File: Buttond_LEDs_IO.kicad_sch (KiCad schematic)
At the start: 16 parts, among them J12 SFH11-PBPC-D05-ST-BK, J13 SFH11-PBPC-D05-ST-BK, SW1 RESET, SW2 BOOT

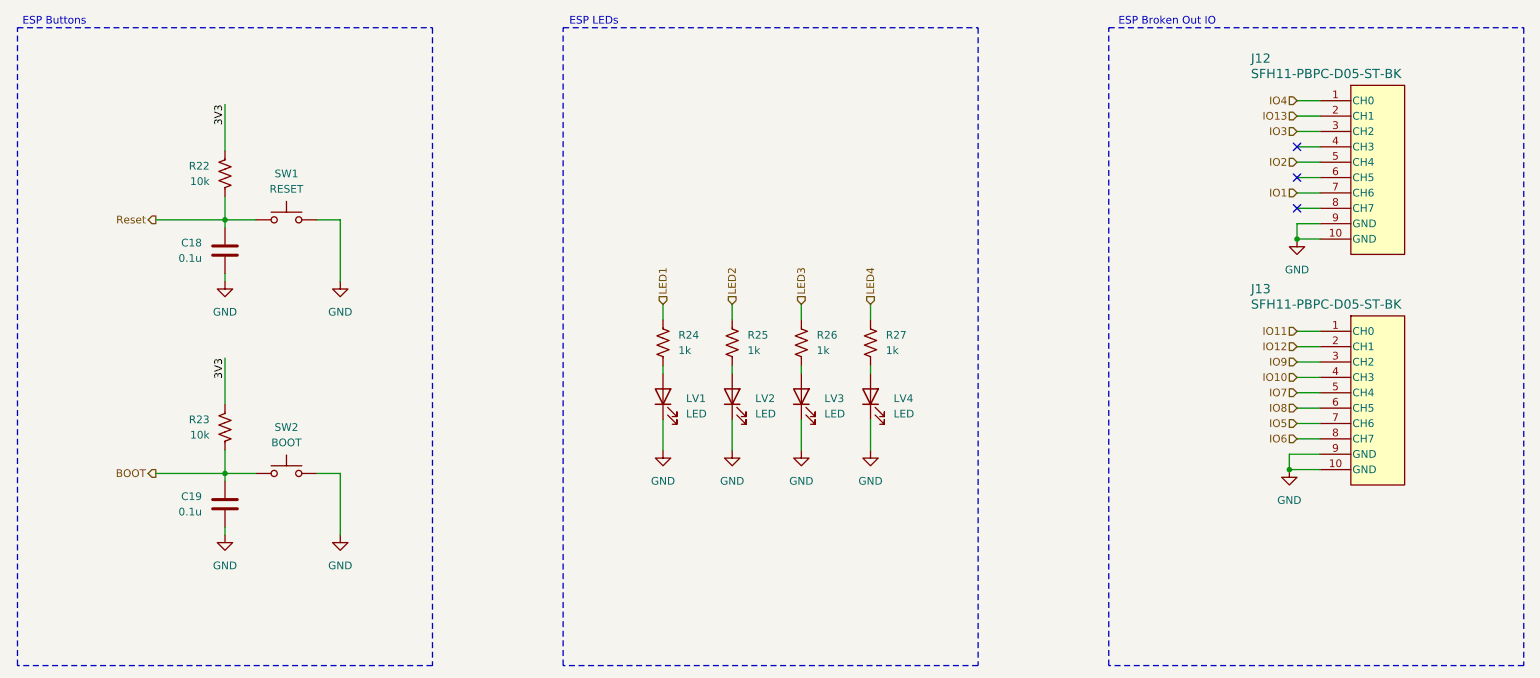
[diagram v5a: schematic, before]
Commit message: changed rpp ic
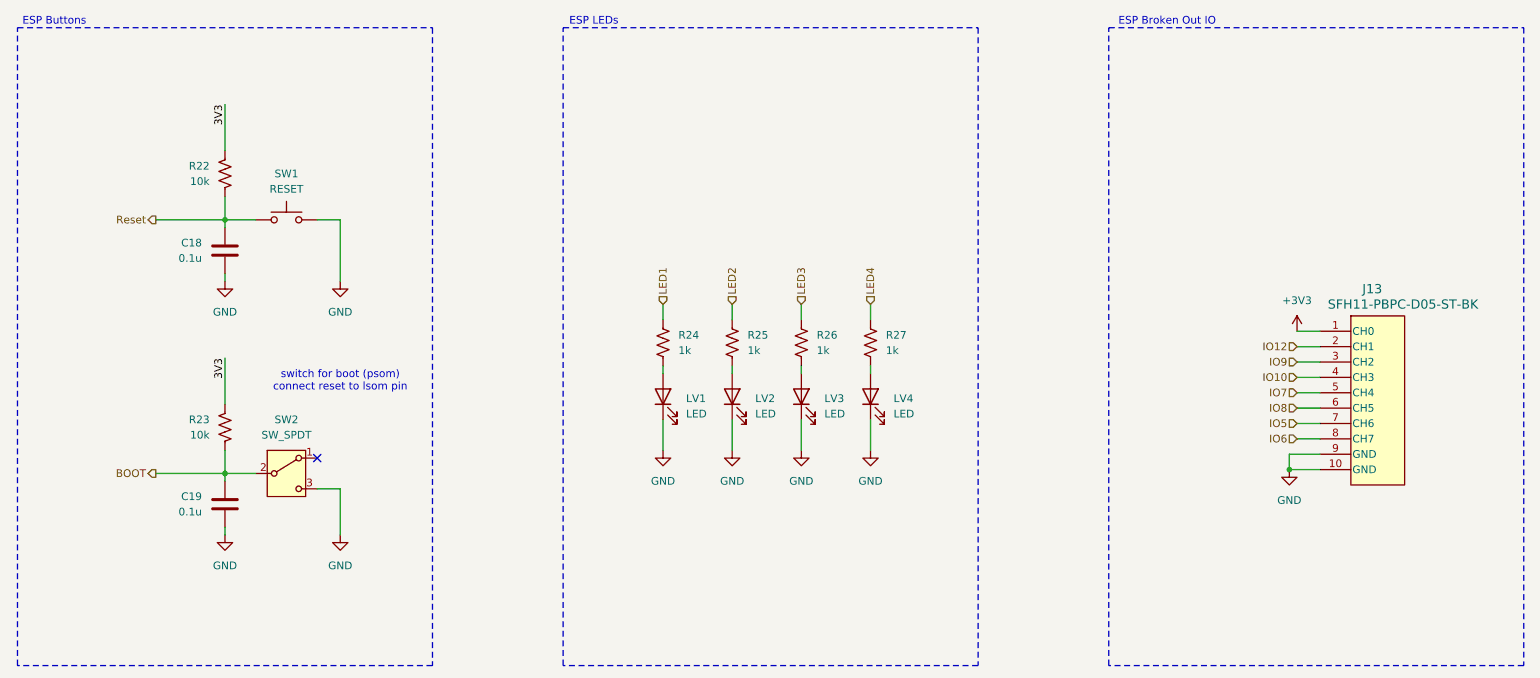
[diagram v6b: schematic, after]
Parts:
- removed J12: SFH11-PBPC-D05-ST-BK, UTSVT_Connectors:CONN_SFH11-xxxC-D05-ST-XX_SUL, symbol UTSVT_Connectors:SFH11-PBPC-D05-ST-BK
- removed SW2: BOOT, UTSVT_Special:SW_SPST_B3SL-1002P, symbol Switch:SW_MEC_5G
- added SW2: SW_SPDT, symbol Switch:SW_SPDT
- J13: P/N (none) -> SFH11-PBPC-D05-ST-BK
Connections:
- net BOOT: now also SW2.2 (B)
- net GND: now also SW2.3 (C)
- net IO11 renamed +3V3
- no-connect marks 3 -> 1
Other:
- note added: "switch for boot (psom) connect reset to lsom pin"

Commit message: as;ldfkjasdl;f
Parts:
- removed C19: 0.1u, Capacitor_SMD:C_0603_1608Metric, symbol Device:C
- SW2: value SW_SPDT -> BOOT; footprint (none) -> UTSVT_Special:SW_CJS-1200TA
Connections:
- net +3V3: now also R22.1, SW2.1 (A)
- net BOOT: now also R23.1; no longer R23.2, SW2.2 (B)
- removed net 3V3: R22.1, R23.1
- new net: R23.2, SW2.2 (B)
- no-connect marks 1 -> 0
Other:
- moved on the sheet: R23
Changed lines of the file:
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@@
-	)
-	(junction
-		(at 60.96 105.41)
-		(diameter 0)
-		(color 0 0 0 0)
 	)
 	(junction
@@
 		(color 0 0 0 0)
 	)
-	(no_connect
-		(at 76.2 102.87)
-	)
 	(wire
 		(pts
@@
 	(wire
 		(pts
-			(xy 60.96 101.6) (xy 60.96 105.41)
-		)
-		(stroke
-			(width 0)
-			(type default)
-		)
-	)
-	(wire
-		(pts
 			(xy 167.64 77.47) (xy 167.64 80.01)
 		)
@@
 	(wire
 		(pts
-			(xy 66.04 105.41) (xy 60.96 105.41)
-		)
-		(stroke
-			(width 0)
-			(type default)
-		)
-	)
-	(wire
-		(pts
 			(xy 167.64 87.63) (xy 167.64 88.9)
 		)
@@
 	(wire
 		(pts
-			(xy 60.96 86.36) (xy 60.96 93.98)
-		)
-		(stroke
-			(width 0)
-			(type default)
-		)
-	)
-	(wire
-		(pts
 			(xy 238.125 84.455) (xy 241.935 84.455)
 		)
@@
 	(wire
 		(pts
-			(xy 60.96 105.41) (xy 49.53 105.41)
-		)
-		(stroke
-			(width 0)
-			(type default)
-		)
-	)
-	(wire
-		(pts
 			(xy 236.855 102.235) (xy 236.855 104.775)
 		)
@@
 	(wire
 		(pts
-			(xy 60.96 114.3) (xy 60.96 115.57)
+			(xy 64.135 105.41) (xy 66.04 105.41)
+		)
+		(stroke
+			(width 0)
+			(type default)
+		)
+	)
+	(wire
+		(pts
+			(xy 49.53 105.41) (xy 56.515 105.41)
 		)
 		(stroke
@@
 	(wire
 		(pts
-			(xy 60.96 105.41) (xy 60.96 106.68)
-		)
-		(stroke
-			(width 0)
-			(type default)
-		)
-	)
-	(wire
-		(pts
 			(xy 238.125 81.915) (xy 241.935 81.915)
 		)
@@
 	(wire
 		(pts
+			(xy 76.2 102.87) (xy 80.01 102.87)
+		)
+		(stroke
+			(width 0)
+			(type default)
+		)
+	)
+	(wire
+		(pts
 			(xy 156.21 77.47) (xy 156.21 80.01)
 		)
@@
 			(width 0)
 			(type default)
-		)
-	)
-	(label "3V3"
-		(at 60.96 44.45 270)
-		(effects
-			(font
-				(size 1.27 1.27)
-			)
-			(justify right bottom)
-		)
-	)
-	(label "3V3"
-		(at 60.96 86.36 270)
-		(effects
-			(font
-				(size 1.27 1.27)
-			)
-			(justify right bottom)
 		)
 	)
@@
 			)
 		)
-		(property "Value" "SW_SPDT"
+		(property "Value" "BOOT"
 			(at 71.12 99.06 0)
 			(effects
@@
 			)
 		)
-		(property "Footprint" ""
+		(property "Footprint" "UTSVT_Special:SW_CJS-1200TA"
 			(at 71.12 105.41 0)
 			(effects
@@
 	)
 	(symbol
-		(lib_id "power:GND")
-		(at 60.96 115.57 0)
-		(mirror y)
-		(unit 1)
-		(exclude_from_sim no)
-		(in_bom yes)
-		(on_board yes)
-		(dnp no)
-		(fields_autoplaced yes)
-		(property "Reference" "#PWR060"
-			(at 60.96 121.92 0)
-			(effects
-				(font
-					(size 1.27 1.27)
-				)
-				(hide yes)
-			)
-		)
-		(property "Value" "GND"
-			(at 60.96 120.65 0)
+		(lib_id "power:+3V3")
+		(at 60.96 44.45 0)
+		(unit 1)
+		(exclude_from_sim no)
+		(in_bom yes)
+		(on_board yes)
+		(dnp no)
+		(fields_autoplaced yes)
+		(property "Reference" "#PWR078"
+			(at 60.96 48.26 0)
+			(effects
+				(font
+					(size 1.27 1.27)
+				)
+				(hide yes)
+			)
+		)
+		(property "Value" "+3V3"
+			(at 60.96 39.37 0)
 			(effects
 				(font
@@
 		)
 		(property "Footprint" ""
-			(at 60.96 115.57 0)
+			(at 60.96 44.45 0)
 			(effects
 				(font
@@
 		)
 		(property "Datasheet" ""
-			(at 60.96 115.57 0)
-			(effects
-				(font
-					(size 1.27 1.27)
-				)
-				(hide yes)
-			)
-		)
-		(property "Description" "Power symbol creates a global label with name \"GND\" , ground"
-			(at 60.96 115.57 0)
-			(effects
-				(font
-					(size 1.27 1.27)
-				)
-				(hide yes)
-			)
-		)
-		(pin "1"
-		)
-		(instances
-			(project "VehicleControlUnit"
-				(path "/795c8e51-3ded-4d21-b864-aaff31c5def7/6282503b-e4ab-454b-a074-f701a067f39b/cecfe08a-2de2-4171-9051-c68b429ab9e8"
-					(reference "#PWR060")
+			(at 60.96 44.45 0)
+			(effects
+				(font
+					(size 1.27 1.27)
+				)
+				(hide yes)
+			)
+		)
+		(property "Description" "Power symbol creates a global label with name \"+3V3\""
+			(at 60.96 44.45 0)
+			(effects
+				(font
+					(size 1.27 1.27)
+				)
+				(hide yes)
+			)
+		)
+		(pin "1"
+		)
+		(instances
+			(project "VehicleControlUnit"
+				(path "/795c8e51-3ded-4d21-b864-aaff31c5def7/6282503b-e4ab-454b-a074-f701a067f39b/cecfe08a-2de2-4171-9051-c68b429ab9e8"
+					(reference "#PWR078")
 					(unit 1)
 				)
@@
 	)
 	(symbol
+		(lib_id "power:+3V3")
+		(at 80.01 102.87 0)
+		(unit 1)
+		(exclude_from_sim no)
+		(in_bom yes)
+		(on_board yes)
+		(dnp no)
+		(fields_autoplaced yes)
+		(property "Reference" "#PWR077"
+			(at 80.01 106.68 0)
+			(effects
+				(font
+					(size 1.27 1.27)
+				)
+				(hide yes)
+			)
+		)
+		(property "Value" "+3V3"
+			(at 80.01 97.79 0)
+			(effects
+				(font
+					(size 1.27 1.27)
+				)
+			)
+		)
+		(property "Footprint" ""
+			(at 80.01 102.87 0)
+			(effects
+				(font
+					(size 1.27 1.27)
+				)
+				(hide yes)
+			)
+		)
+		(property "Datasheet" ""
+			(at 80.01 102.87 0)
+			(effects
+				(font
+					(size 1.27 1.27)
+				)
+				(hide yes)
+			)
+		)
+		(property "Description" "Power symbol creates a global label with name \"+3V3\""
+			(at 80.01 102.87 0)
+			(effects
+				(font
+					(size 1.27 1.27)
+				)
+				(hide yes)
+			)
+		)
+		(pin "1"
+		)
+		(instances
+			(project "VehicleControlUnit"
+				(path "/795c8e51-3ded-4d21-b864-aaff31c5def7/6282503b-e4ab-454b-a074-f701a067f39b/cecfe08a-2de2-4171-9051-c68b429ab9e8"
+					(reference "#PWR077")
+					(unit 1)
+				)
+			)
+		)
+	)
+	(symbol
 		(lib_id "Device:R_US")
 		(at 144.78 83.82 0)
@@
 	(symbol
 		(lib_id "Device:R_US")
-		(at 60.96 97.79 0)
-		(mirror y)
+		(at 60.325 105.41 90)
+		(mirror x)
 		(unit 1)
 		(exclude_from_sim no)
@@
 		(fields_autoplaced yes)
 		(property "Reference" "R23"
-			(at 58.42 96.5199 0)
-			(effects
-				(font
-					(size 1.27 1.27)
-				)
-				(justify left)
+			(at 60.325 99.06 90)
+			(effects
+				(font
+					(size 1.27 1.27)
+				)
 			)
 		)
 		(property "Value" "10k"
-			(at 58.42 99.0599 0)
-			(effects
-				(font
-					(size 1.27 1.27)
-				)
-				(justify left)
+			(at 60.325 101.6 90)
+			(effects
+				(font
+					(size 1.27 1.27)
+				)
 			)
 		)
 		(property "Footprint" "Resistor_SMD:R_0603_1608Metric"
-			(at 59.944 98.044 90)
+			(at 60.579 106.426 90)
 			(effects
 				(font
@@
 		)
 		(property "Datasheet" "~"
-			(at 60.96 97.79 0)
+			(at 60.325 105.41 0)
 			(effects
 				(font
@@
 		)
 		(property "Description" "Resistor, US symbol"
-			(at 60.96 97.79 0)
+			(at 60.325 105.41 0)
 			(effects
 				(font
@@
 					(unit 1)
 				)
-			)
-		)
-	)
-	(symbol
-		(lib_id "Device:C")
-		(at 60.96 110.49 0)
-		(mirror y)
-		(unit 1)
-		(exclude_from_sim no)
-		(in_bom yes)
-		(on_board yes)
-		(dnp no)
-		(fields_autoplaced yes)
-		(property "Reference" "C19"
-			(at 57.15 109.2199 0)
-			(effects
-				(font
-					(size 1.27 1.27)
-				)
-				(justify left)
-			)
-		)
-		(property "Value" "0.1u"
-			(at 57.15 111.7599 0)
-			(effects
-				(font
-					(size 1.27 1.27)
-				)
-				(justify left)
-			)
-		)
-		(property "Footprint" "Capacitor_SMD:C_0603_1608Metric"
-			(at 59.9948 114.3 0)
-			(effects
-				(font
-					(size 1.27 1.27)
-				)
-				(hide yes)
-			)
-		)
-		(property "Datasheet" "~"
-			(at 60.96 110.49 0)
-			(effects
-				(font
-					(size 1.27 1.27)
-				)
-				(hide yes)
-			)
-		)
-		(property "Description" "Unpolarized capacitor"
-			(at 60.96 110.49 0)
-			(effects
-				(font
-					(size 1.27 1.27)
-				)
-				(hide yes)
-			)
-		)
-		(pin "1"
-		)
-		(pin "2"
-		)
-		(instances
-			(project "VehicleControlUnit"
-				(path "/795c8e51-3ded-4d21-b864-aaff31c5def7/6282503b-e4ab-454b-a074-f701a067f39b/cecfe08a-2de2-4171-9051-c68b429ab9e8"
-					(reference "C19")
-					(unit 1)
-				)

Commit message: lakshay edits
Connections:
- net +3V3: no longer J13.1 (CH0)
- net IO10: now also J13.1 (CH0); no longer J13.4 (CH3)
- net IO5: now also J13.8 (CH7); no longer J13.7 (CH6)
- net IO6: now also J13.5 (CH4); no longer J13.8 (CH7)
- net IO7: now also J13.6 (CH5); no longer J13.5 (CH4)
- net IO8: now also J13.3 (CH2); no longer J13.6 (CH5)
- net IO9: now also J13.4 (CH3); no longer J13.3 (CH2)
- new net IO4: J13.7 (CH6)
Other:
- moved on the sheet: LV1, LV2, LV3, LV4, R24, R25, R26, R27
